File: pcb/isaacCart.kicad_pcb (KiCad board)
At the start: 2 copper layers, 51.4 x 61 mm, 5 parts, among them J1 CartBus, U1 AT28C256

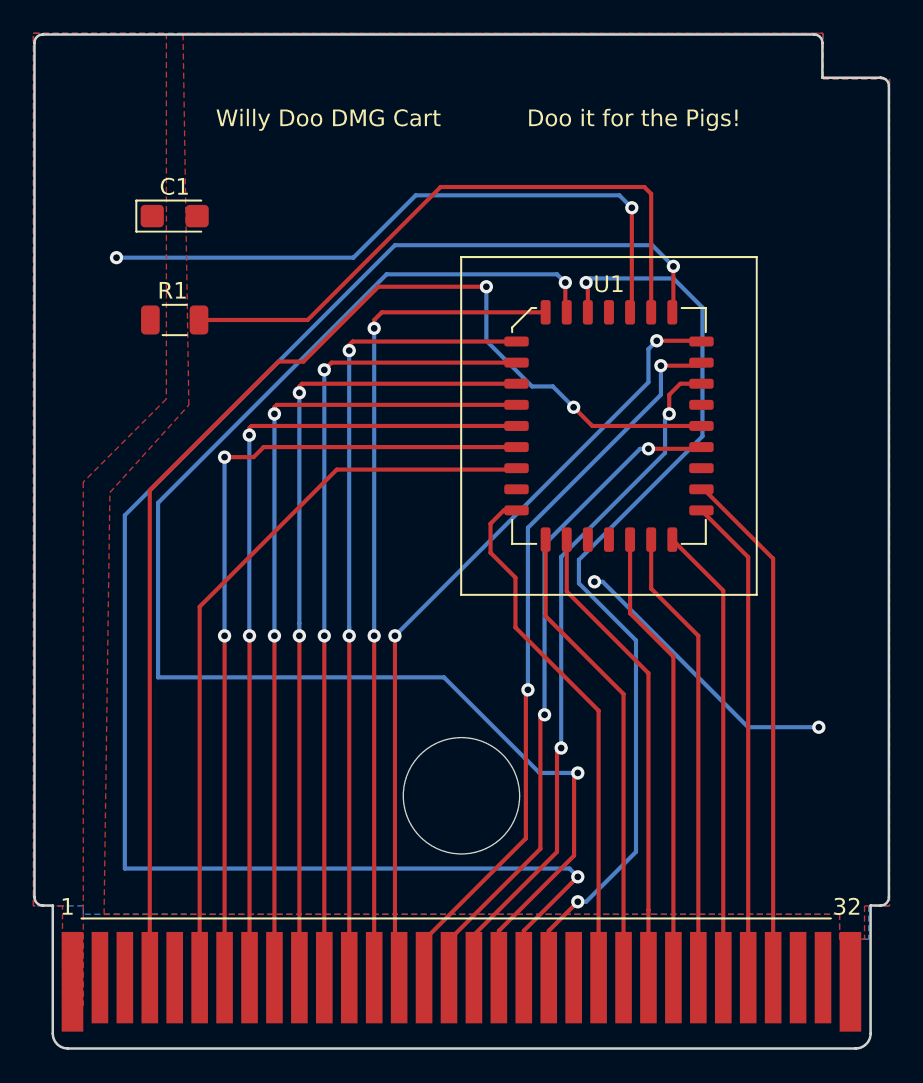
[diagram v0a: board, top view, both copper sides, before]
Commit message: New schematic + Board layout based on SST39SF020 PLCC-32 flash chip layout
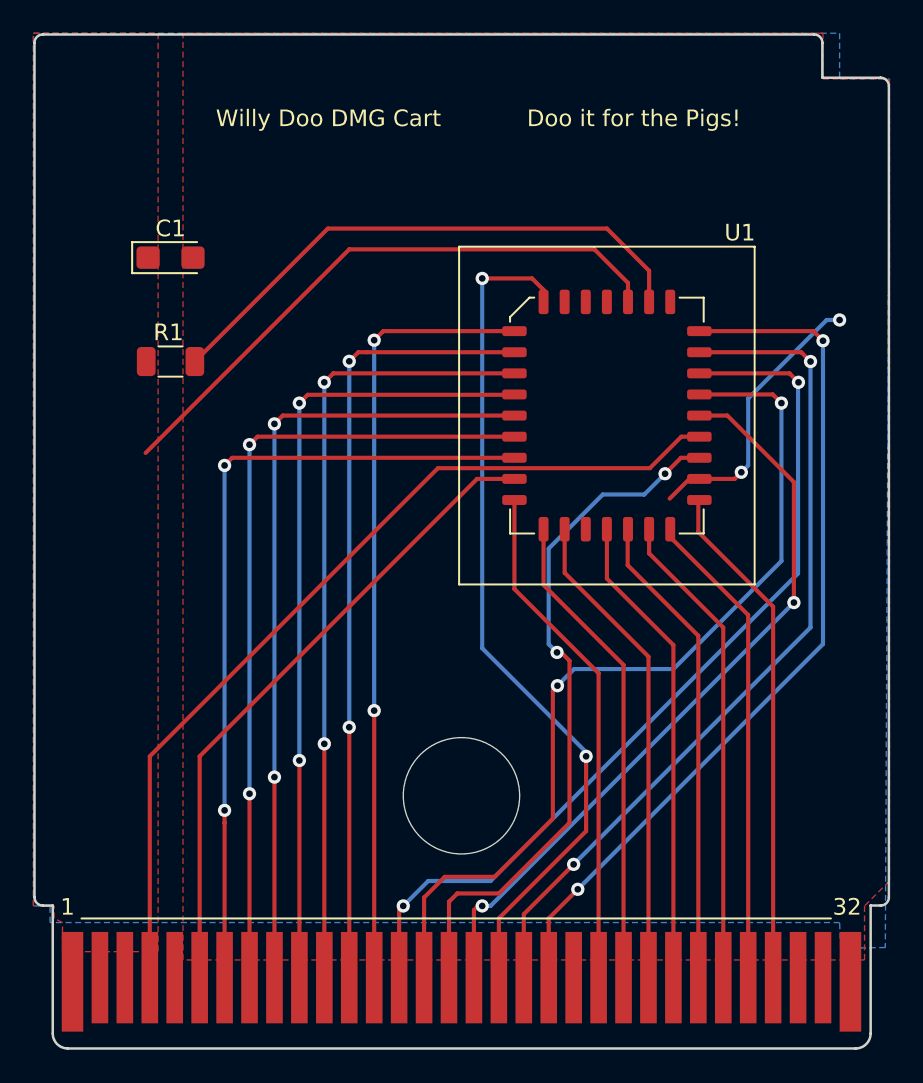
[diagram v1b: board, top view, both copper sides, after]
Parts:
- U1: value AT28C256 -> SST39SF020
- moved C1 2.51 mm to (111.2, 91.6)
- moved R1 2.51 mm to (111.2, 97.9)
- moved U1 0.64 mm to (137.4, 101.1)
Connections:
- U1 pad 1: (no net) -> unconnected-(U1-Pad1)
- U1 pad 10: A1 -> A2
- U1 pad 11: A0 -> A1
- U1 pad 12: (no net) -> A0
- U1 pad 17: (no net) -> D3
- U1 pad 18: D3 -> D4
- U1 pad 19: D4 -> D5
- U1 pad 2: A14 -> unconnected-(U1-Pad2)
- U1 pad 20: D5 -> D6
- U1 pad 21: D6 -> D7
- U1 pad 22: D7 -> GND
- U1 pad 23: GND -> A10
- U1 pad 24: A10 -> GBRD
- U1 pad 25: GBRD -> A11
- U1 pad 26: (no net) -> A9
- U1 pad 27: A11 -> A8
- U1 pad 28: A9 -> A13
- U1 pad 29: A8 -> A14
- U1 pad 3: A12 -> unconnected-(U1-Pad3)
- U1 pad 30: A13 -> unconnected-(U1-Pad30)
- U1 pad 4: A7 -> A12
- U1 pad 5: A6 -> A7
- U1 pad 6: A5 -> A6
- U1 pad 7: A4 -> A5
- U1 pad 8: A3 -> A4
- U1 pad 9: A2 -> A3
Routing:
- net A13: track 99.2 -> 51.1 mm
- net A12: track 84.6 -> 51.5 mm
- net GBRD: track 72.9 -> 54.3 mm, vias 2 -> 0
- net A9: track 45.2 -> 53.9 mm
- net A8: track 47.6 -> 54.1 mm
- net A0: track 44.8 -> 39.2 mm
- net Net-(R1-Pad1): track 37.8 -> 33.6 mm
- net A14: track 56.9 -> 52.8 mm
- net A11: track 42.1 -> 45.6 mm
- net +5V: track 39.2 -> 36.1 mm, vias 2 -> 0
- net A7: track 50.1 -> 47.0 mm
- net A10: track 40.3 -> 42.3 mm
- net D4: track 27.5 -> 28.7 mm
- net D5: track 27.6 -> 28.8 mm
- net D3: track 27.4 -> 28.6 mm
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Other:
- board text added: "Designed By: Isaac Flaum Rev. 2.0 Flash"
- board text removed: "Designed By: Isaac Flaum Rev. 1.0"
